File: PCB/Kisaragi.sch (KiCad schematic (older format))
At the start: 106 parts, among them SW1 SW_PUSH, SW10 SW_PUSH, SW11 SW_PUSH, SW12 SW_PUSH, SW13 SW_PUSH, SW14 SW_PUSH, SW15 SW_PUSH, SW16 SW_PUSH, SW17 SW_PUSH, SW18 SW_PUSH, SW19 SW_PUSH, SW2 SW_PUSH, SW20 SW_PUSH, SW21 SW_PUSH, SW22 SW_PUSH, SW23 SW_PUSH, SW24 SW_PUSH, SW25 SW_PUSH, SW26 SW_PUSH, SW27 SW_PUSH, SW28 SW_PUSH, SW29 SW_PUSH, SW3 SW_PUSH, SW30 SW_PUSH, SW31 SW_PUSH, SW32 SW_PUSH, SW33 SW_PUSH, SW34 SW_PUSH, SW35 SW_PUSH, SW36 SW_PUSH, SW37 SW_PUSH, SW38 SW_PUSH, SW39 SW_PUSH, SW4 SW_PUSH, SW40 SW_PUSH, SW41 SW_PUSH, SW42 SW_PUSH, SW43 SW_PUSH, SW44 SW_PUSH, SW45 SW_PUSH, SW46 SW_PUSH, SW47 SW_PUSH, SW48 SW_PUSH, SW49 SW_PUSH, SW5 SW_PUSH, SW50 SW_PUSH, SW51 SW_PUSH, SW52 SW_PUSH, SW53 reset, SW6 SW_PUSH, SW7 SW_PUSH, SW8 SW_PUSH, SW9 SW_PUSH, U1 ProMicro

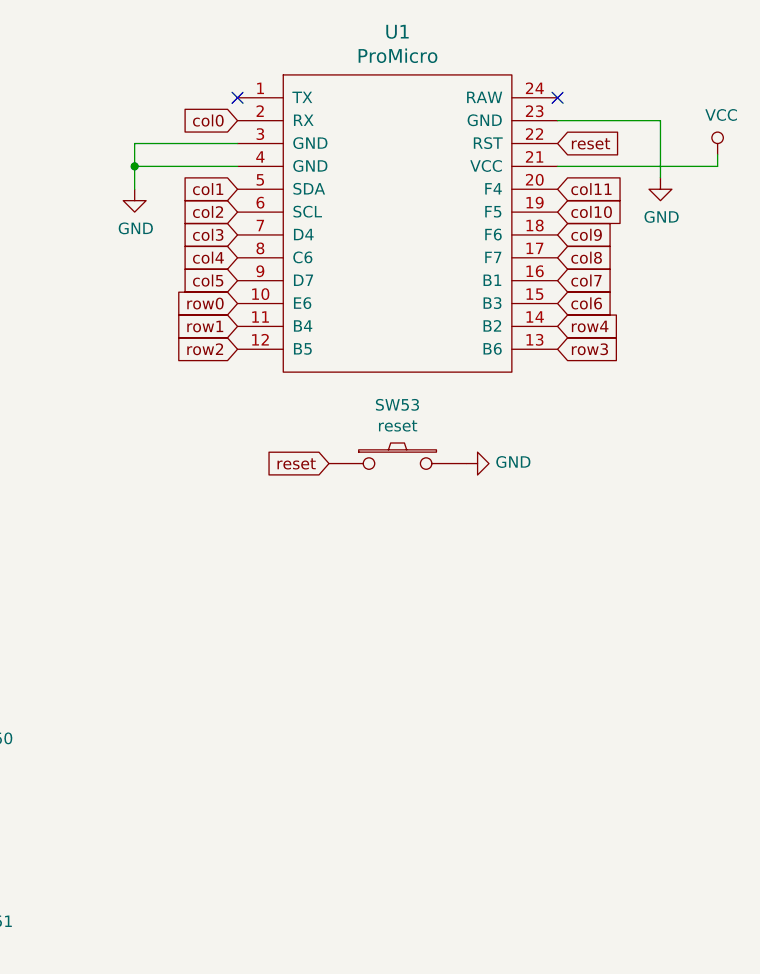
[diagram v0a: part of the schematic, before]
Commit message: added LED strip support
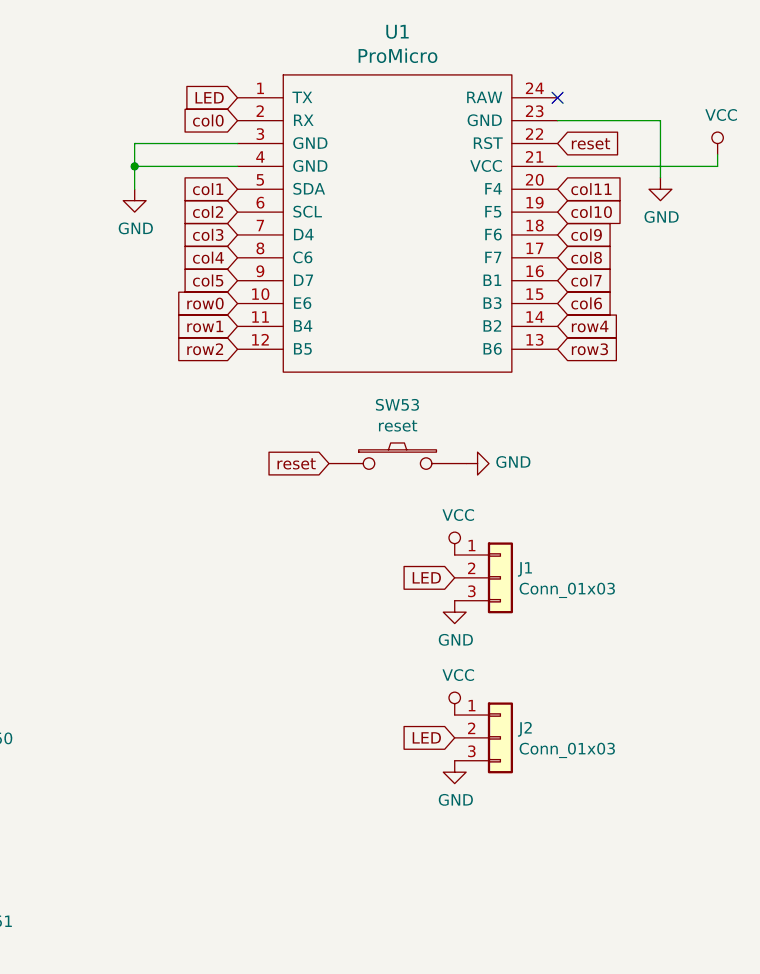
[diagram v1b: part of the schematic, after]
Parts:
- added J1, J2: Conn_01x03, kbd:LEDStrip, symbol Connector_Generic:Conn_01x03
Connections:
- net GND: now also J1.3 (Pin_3), J2.3 (Pin_3)
- net VCC: now also J1.1 (Pin_1), J2.1 (Pin_1)
- net LED: now reaches U1.1 (TX)
- net LED: now also J1.2 (Pin_2), J2.2 (Pin_2)
- no-connect marks 2 -> 1
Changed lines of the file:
@@
 EESchema Schematic File Version 4
-LIBS:KBS52-cache
+LIBS:Kisaragi-cache
 EELAYER 26 0
 EELAYER END
@@
 col0
 NoConn ~ 14700 1100
-NoConn ~ 13300 1100
 $Comp
 L power:PWR_FLAG #FLG0101
@@
 	1    0    0    -1
 $EndComp
+$Comp
+L Connector_Generic:Conn_01x03 J1
+U 1 1 5C73A179
+P 14450 3200
+F 0 "J1" H 14530 3242 50  0000 L CNN
+F 1 "Conn_01x03" H 14530 3151 50  0000 L CNN
+F 2 "kbd:LEDStrip" H 14450 3200 50  0001 C CNN
+F 3 "~" H 14450 3200 50  0001 C CNN
+	1    14450 3200
+	1    0    0    -1
+$EndComp
+$Comp
+L Atreus62-cache:VCC #PWR0101
+U 1 1 5C73A41F
+P 14250 3100
+F 0 "#PWR0101" H 14250 2950 50  0001 C CNN
+F 1 "VCC" H 14267 3273 50  0000 C CNN
+F 2 "" H 14250 3100 50  0000 C CNN
+F 3 "" H 14250 3100 50  0000 C CNN
+	1    14250 3100
+	1    0    0    -1
+$EndComp
+$Comp
+L Atreus62-cache:GND #PWR0102
+U 1 1 5C73A52C
+P 14250 3300
+F 0 "#PWR0102" H 14250 3050 50  0001 C CNN
+F 1 "GND" H 14255 3127 50  0000 C CNN
+F 2 "" H 14250 3300 50  0000 C CNN
+F 3 "" H 14250 3300 50  0000 C CNN
+	1    14250 3300
+	1    0    0    -1
+$EndComp
+Text GLabel 14250 3200 0    50   Input ~ 0
+LED
+Text GLabel 13300 1100 0    50   Input ~ 0
+LED
+$Comp
+L Connector_Generic:Conn_01x03 J2
+U 1 1 5C73EE55
+P 14450 3900
+F 0 "J2" H 14530 3942 50  0000 L CNN
+F 1 "Conn_01x03" H 14530 3851 50  0000 L CNN
+F 2 "kbd:LEDStrip" H 14450 3900 50  0001 C CNN
+F 3 "~" H 14450 3900 50  0001 C CNN
+	1    14450 3900
+	1    0    0    -1
+$EndComp
+$Comp
+L Atreus62-cache:VCC #PWR0105
+U 1 1 5C73EE5C
+P 14250 3800
+F 0 "#PWR0105" H 14250 3650 50  0001 C CNN
+F 1 "VCC" H 14267 3973 50  0000 C CNN
+F 2 "" H 14250 3800 50  0000 C CNN
+F 3 "" H 14250 3800 50  0000 C CNN
+	1    14250 3800
+	1    0    0    -1
+$EndComp
+$Comp
+L Atreus62-cache:GND #PWR0106
+U 1 1 5C73EE62
+P 14250 4000
+F 0 "#PWR0106" H 14250 3750 50  0001 C CNN
+F 1 "GND" H 14255 3827 50  0000 C CNN
+F 2 "" H 14250 4000 50  0000 C CNN
+F 3 "" H 14250 4000 50  0000 C CNN
+	1    14250 4000
+	1    0    0    -1
+$EndComp
+Text GLabel 14250 3900 0    50   Input ~ 0
+LED
 $EndSCHEMATC
